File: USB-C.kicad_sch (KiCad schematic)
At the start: 8 parts, among them J2 HRO_TYPE-C-31-M-12, U3 USBLC6-2SC6

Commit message: feat(pcb): Version 0.2
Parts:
- removed U3: USBLC6-2SC6, marbastlib-various:SOT-23-6-routable, symbol Power_Protection:USBLC6-2SC6
- added U3: (no value), symbol Power_Protection:SRV05-4
- C8: value 4.7uF -> (none); footprint Capacitor_SMD:C_0603_1608Metric -> (none)
- C9: value 1uF -> (none); footprint Capacitor_SMD:C_0603_1608Metric -> (none)
- F2: value 500mA -> (none); footprint Fuse:Fuse_0603_1608Metric -> (none)
- FB1: value 120@100MHz -> (none); footprint Inductor_SMD:L_0603_1608Metric -> (none)
- J2: value HRO_TYPE-C-31-M-12 -> (none); footprint Conejo:USB_C_Receptacle_HRO_TYPE-C-31-M-12 (Reversible) -> (none)
- R8: renamed from R9; value 5K1 -> (none); footprint Resistor_SMD:R_0603_1608Metric -> (none)
- R9: renamed from R10; value 5K1 -> (none); footprint Resistor_SMD:R_0603_1608Metric -> (none)
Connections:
- net +5V: now also U3.5 (VP)
- net GND: now also U3.2 (VN)
- net DI+ renamed D+
- net D+: now also U3.4 (IO3)
- net DI- renamed D-
- net D-: now also U3.3 (IO2)

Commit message: feat(pcb): Version 0.2.1
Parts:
- C8: value (none) -> 4.7uF; footprint (none) -> Capacitor_SMD:C_0402_1005Metric
- C9: value (none) -> 1uF; footprint (none) -> Capacitor_SMD:C_0402_1005Metric
- FB1: value (none) -> 120@100MHz; footprint (none) -> Inductor_SMD:L_0402_1005Metric
- J2: value (none) -> HRO_TYPE-C-31-M-12; footprint (none) -> Athena54:USB_C_Receptacle_HRO_TYPE-C-31-M-12 (Reversible)
- R8, R9: value (none) -> 5K1; footprint (none) -> Resistor_SMD:R_0402_1005Metric
- U3: value (none) -> SRV05-4; footprint (none) -> marbastlib-various:SOT-23-6-routable
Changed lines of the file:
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@@
       (effects (font (size 1.27 1.27)) (justify right))
     )
-    (property "Value" "" (id 1) (at 75.3491 34.7158 0)
-      (effects (font (size 1.27 1.27)) (justify right))
-    )
-    (property "Footprint" "" (id 2) (at 73.025 33.02 0)
+    (property "Value" "4.7uF" (id 1) (at 75.3491 34.7158 0)
+      (effects (font (size 1.27 1.27)) (justify right))
+    )
+    (property "Footprint" "Capacitor_SMD:C_0402_1005Metric" (id 2) (at 73.025 33.02 0)
       (effects (font (size 1.27 1.27)) hide)
     )
@@
       (effects (font (size 1.27 1.27)) (justify right))
     )
-    (property "Value" "" (id 1) (at 88.0491 34.7158 0)
-      (effects (font (size 1.27 1.27)) (justify right))
-    )
-    (property "Footprint" "" (id 2) (at 85.725 33.02 0)
+    (property "Value" "1uF" (id 1) (at 88.0491 34.7158 0)
+      (effects (font (size 1.27 1.27)) (justify right))
+    )
+    (property "Footprint" "Capacitor_SMD:C_0402_1005Metric" (id 2) (at 85.725 33.02 0)
       (effects (font (size 1.27 1.27)) hide)
     )
@@
       (effects (font (size 1.27 1.27)) (justify left))
     )
-    (property "Value" "" (id 1) (at 120.2437 29.3171 0)
-      (effects (font (size 1.27 1.27)) (justify left))
-    )
-    (property "Footprint" "" (id 2) (at 135.255 52.07 0)
+    (property "Value" "SRV05-4" (id 1) (at 120.2437 29.3171 0)
+      (effects (font (size 1.27 1.27)) (justify left))
+    )
+    (property "Footprint" "marbastlib-various:SOT-23-6-routable" (id 2) (at 135.255 52.07 0)
       (effects (font (size 1.27 1.27)) hide)
     )
@@
       (effects (font (size 1.27 1.27)) (justify left))
     )
-    (property "Value" "" (id 1) (at 64.9986 41.7072 0)
-      (effects (font (size 1.27 1.27)) (justify left))
-    )
-    (property "Footprint" "" (id 2) (at 63.5 40.005 0)
+    (property "Value" "5K1" (id 1) (at 64.9986 41.7072 0)
+      (effects (font (size 1.27 1.27)) (justify left))
+    )
+    (property "Footprint" "Resistor_SMD:R_0402_1005Metric" (id 2) (at 63.5 40.005 0)
       (effects (font (size 1.27 1.27)) hide)
     )
@@
       (effects (font (size 1.27 1.27)) (justify right))
     )
-    (property "Value" "" (id 1) (at 58.8264 41.7072 0)
-      (effects (font (size 1.27 1.27)) (justify right))
-    )
-    (property "Footprint" "" (id 2) (at 60.325 40.005 0)
+    (property "Value" "5K1" (id 1) (at 58.8264 41.7072 0)
+      (effects (font (size 1.27 1.27)) (justify right))
+    )
+    (property "Footprint" "Resistor_SMD:R_0402_1005Metric" (id 2) (at 60.325 40.005 0)
       (effects (font (size 1.27 1.27)) hide)
     )
@@
     (in_bom yes) (on_board yes) (fields_autoplaced)
     (property "Reference" "J2" (id 0) (at 26.67 22.3352 0))
-    (property "Value" "" (id 1) (at 26.67 24.8721 0))
-    (property "Footprint" "" (id 2) (at 30.48 43.815 0)
+    (property "Value" "HRO_TYPE-C-31-M-12" (id 1) (at 26.67 24.8721 0))
+    (property "Footprint" "Athena54:USB_C_Receptacle_HRO_TYPE-C-31-M-12 (Reversible)" (id 2) (at 30.48 43.815 0)
       (effects (font (size 1.27 1.27)) hide)
     )
@@
     (in_bom yes) (on_board yes) (fields_autoplaced)
     (property "Reference" "FB1" (id 0) (at 63.4619 23.1734 90))
-    (property "Value" "" (id 1) (at 63.4619 25.7103 90))
-    (property "Footprint" "" (id 2) (at 63.5 30.353 90)
-      (effects (font (size 1.27 1.27)) hide)
-    )
+    (property "Value" "120@100MHz" (id 1) (at 63.4619 25.7103 90))
+    (property "Footprint" "Inductor_SMD:L_0402_1005Metric" (id 2) (at 63.5 30.353 90)
+      (effects (font (size 1.27 1.27)) hide)
+    )

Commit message: fix(schematic): Fix links to footprints
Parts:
- F2: value (none) -> 500mA; footprint (none) -> Fuse:Fuse_0603_1608Metric
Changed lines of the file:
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@@
     (in_bom yes) (on_board yes) (fields_autoplaced)
     (property "Reference" "F2" (id 0) (at 50.8 23.9862 90))
-    (property "Value" "" (id 1) (at 50.8 26.5231 90))
-    (property "Footprint" "" (id 2) (at 55.88 27.305 0)
+    (property "Value" "500mA" (id 1) (at 50.8 26.5231 90))
+    (property "Footprint" "Fuse:Fuse_0603_1608Metric" (id 2) (at 55.88 27.305 0)
       (effects (font (size 1.27 1.27)) (justify left) hide)
     )

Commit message: refactor!!!(repository): Rename from Athena54 to Conejo
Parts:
- J2: footprint Athena54:USB_C_Receptacle_HRO_TYPE-C-31-M-12 (Reversible) -> Conejo:USB_C_Receptacle_HRO_TYPE-C-31-M-12 (Reversible)
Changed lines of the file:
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@@
     (property "Reference" "J2" (id 0) (at 26.67 22.3352 0))
     (property "Value" "HRO_TYPE-C-31-M-12" (id 1) (at 26.67 24.8721 0))
-    (property "Footprint" "Athena54:USB_C_Receptacle_HRO_TYPE-C-31-M-12 (Reversible)" (id 2) (at 30.48 43.815 0)
+    (property "Footprint" "Conejo:USB_C_Receptacle_HRO_TYPE-C-31-M-12 (Reversible)" (id 2) (at 30.48 43.815 0)
       (effects (font (size 1.27 1.27)) hide)
     )

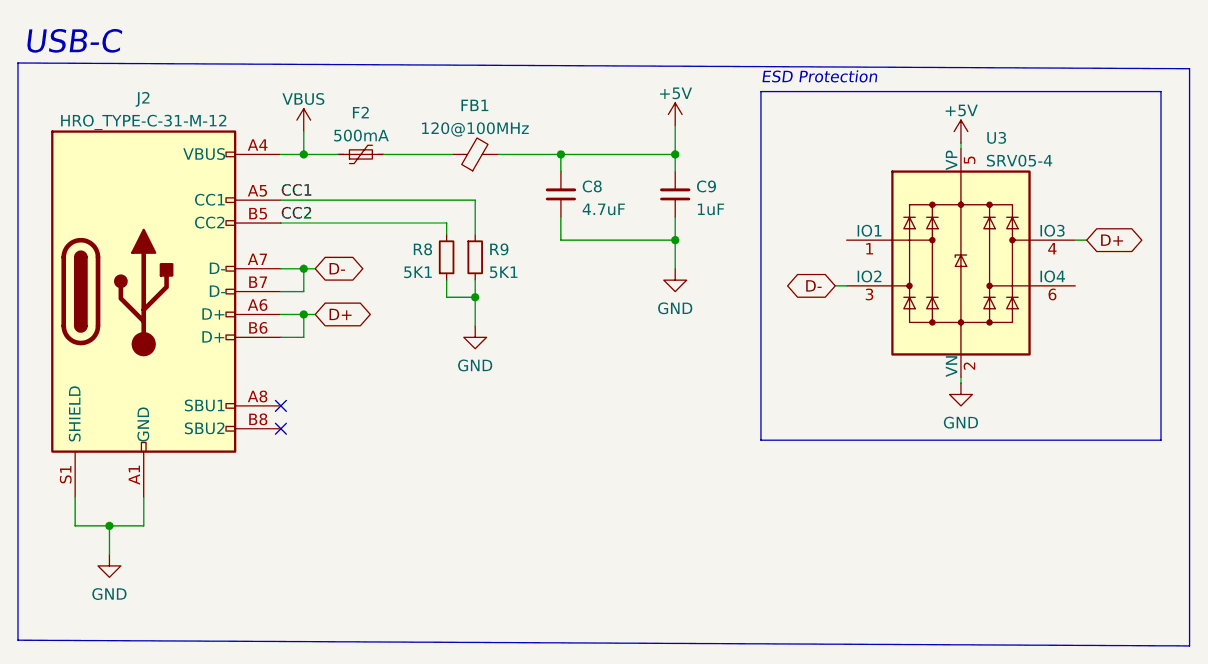
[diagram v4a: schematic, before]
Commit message: feat(pcb): Version 0.2.2
- Update MS88SF3 footprint
- Create thumb cluster silksscreen
- Separate NTPH and PTH drill files
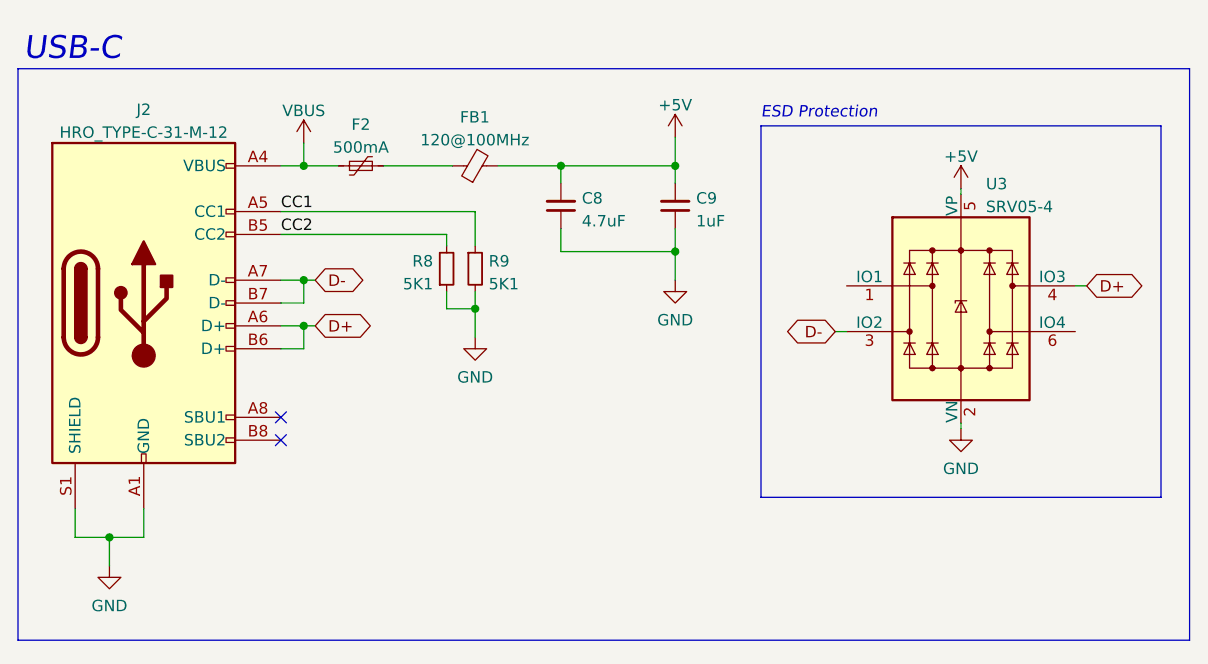
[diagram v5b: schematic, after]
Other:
- moved on the sheet: C8, C9, F2, FB1, J2, R8, R9, U3

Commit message: feat(pcb): Version 0.3
- Move components entirely to back copper :tada:
- Update silkscreen legibility to enhance ease of component placement
- Fix I2C pullup resistors
  - Replace incorrect value of 1K5 with 5K1
  - Update footprint to 0603_1608 to fit VDD traces underneath, compared to original 0402_1005 footprint
- Increase text width on RESET button, POWER Switch, and CHG LED
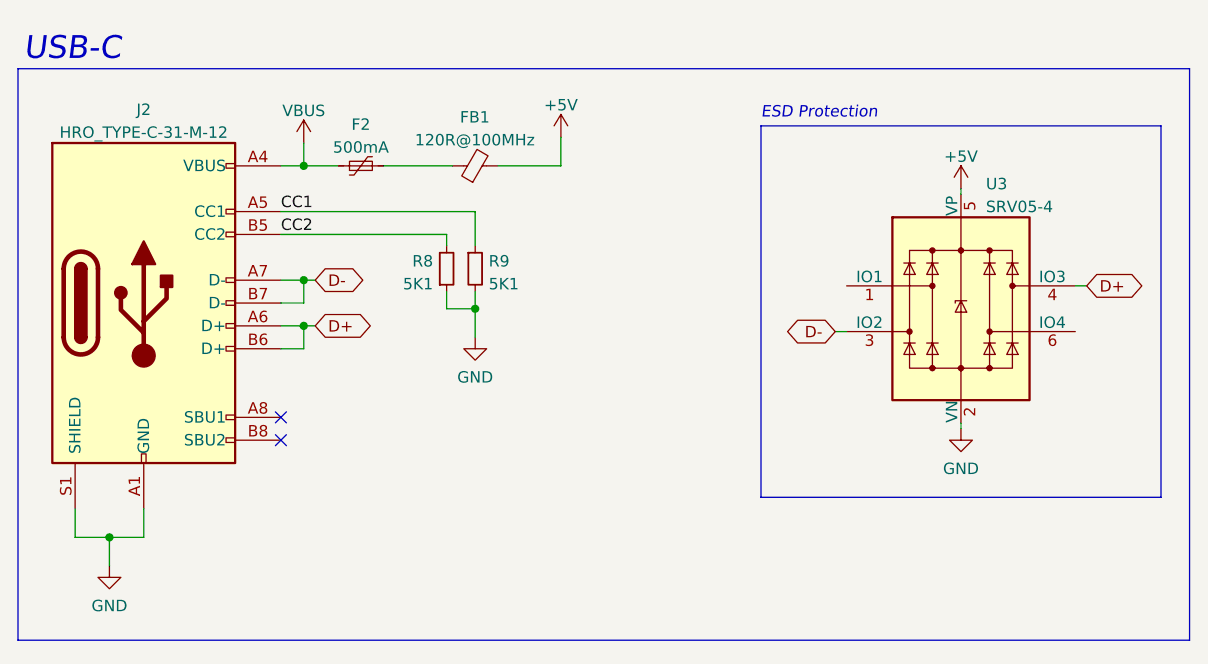
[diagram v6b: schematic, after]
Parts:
- removed C8: 4.7uF, Capacitor_SMD:C_0402_1005Metric, symbol Device:C_Small
- removed C9: 1uF, Capacitor_SMD:C_0402_1005Metric, symbol Device:C_Small
- FB1: value 120@100MHz -> 120R@100MHz
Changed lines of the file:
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@@
   (junction (at 44.45 47.625) (diameter 0) (color 0 0 0 0)
   )
-  (junction (at 73.025 29.845) (diameter 0) (color 0 0 0 0)
-  )
   (junction (at 44.45 42.545) (diameter 0) (color 0 0 0 0)
   )
-  (junction (at 85.725 39.37) (diameter 0) (color 0 0 0 0)
-  )
   (junction (at 63.5 45.72) (diameter 0) (color 0 0 0 0)
   )
   (junction (at 44.45 29.845) (diameter 0) (color 0 0 0 0)
-  )
-  (junction (at 85.725 29.845) (diameter 0) (color 0 0 0 0)
   )
   (junction (at 22.86 71.12) (diameter 0) (color 0 0 0 0)
@@
     (stroke (width 0) (type default) (color 0 0 0 0))
   )
-  (wire (pts (xy 85.725 29.845) (xy 85.725 26.67))
-    (stroke (width 0) (type default) (color 0 0 0 0))
-  )
-  (wire (pts (xy 73.025 39.37) (xy 85.725 39.37))
+  (wire (pts (xy 73.025 29.845) (xy 73.025 26.67))
     (stroke (width 0) (type default) (color 0 0 0 0))
   )
@@
     (stroke (width 0) (type default) (color 0 0 0 0))
   )
-  (wire (pts (xy 85.725 29.845) (xy 85.725 31.75))
-    (stroke (width 0) (type default) (color 0 0 0 0))
-  )
   (wire (pts (xy 41.91 47.625) (xy 44.45 47.625))
     (stroke (width 0) (type default) (color 0 0 0 0))
   )
-  (wire (pts (xy 73.025 29.845) (xy 85.725 29.845))
-    (stroke (width 0) (type default) (color 0 0 0 0))
-  )
   (wire (pts (xy 53.34 29.845) (xy 60.96 29.845))
     (stroke (width 0) (type default) (color 0 0 0 0))
@@
     (stroke (width 0) (type default) (color 0 0 0 0))
   )
-  (wire (pts (xy 73.025 36.83) (xy 73.025 39.37))
-    (stroke (width 0) (type default) (color 0 0 0 0))
-  )
   (polyline (pts (xy 95.25 66.675) (xy 95.25 25.4))
     (stroke (width 0) (type default) (color 0 0 0 0))
@@
     (stroke (width 0) (type default) (color 0 0 0 0))
   )
-  (wire (pts (xy 85.725 42.545) (xy 85.725 39.37))
-    (stroke (width 0) (type default) (color 0 0 0 0))
-  )
   (wire (pts (xy 117.475 32.385) (xy 117.475 33.02))
     (stroke (width 0) (type default) (color 0 0 0 0))
@@
   )
   (wire (pts (xy 60.325 45.72) (xy 63.5 45.72))
-    (stroke (width 0) (type default) (color 0 0 0 0))
-  )
-  (wire (pts (xy 73.025 29.845) (xy 73.025 31.75))
-    (stroke (width 0) (type default) (color 0 0 0 0))
-  )
-  (wire (pts (xy 85.725 36.83) (xy 85.725 39.37))
     (stroke (width 0) (type default) (color 0 0 0 0))
   )
@@
     )
   )
-  (symbol (lib_id "Device:C_Small") (at 73.025 34.29 180) (unit 1)
-    (in_bom yes) (on_board yes)
-    (property "Reference" "C8" (id 0) (at 75.3491 33.4489 0)
-      (effects (font (size 1.27 1.27)) (justify right))
-    )
-    (property "Value" "4.7uF" (id 1) (at 75.3491 35.9858 0)
-      (effects (font (size 1.27 1.27)) (justify right))
-    )
-    (property "Footprint" "Capacitor_SMD:C_0402_1005Metric" (id 2) (at 73.025 34.29 0)
-      (effects (font (size 1.27 1.27)) hide)
-    )
-    (property "Datasheet" "~" (id 3) (at 73.025 34.29 0)
-      (effects (font (size 1.27 1.27)) hide)
-    )
-    (pin "1")
-    (pin "2")
-  )
-  (symbol (lib_id "Device:C_Small") (at 85.725 34.29 180) (unit 1)
-    (in_bom yes) (on_board yes) (fields_autoplaced)
-    (property "Reference" "C9" (id 0) (at 88.0491 33.4489 0)
-      (effects (font (size 1.27 1.27)) (justify right))
-    )
-    (property "Value" "1uF" (id 1) (at 88.0491 35.9858 0)
-      (effects (font (size 1.27 1.27)) (justify right))
-    )
-    (property "Footprint" "Capacitor_SMD:C_0402_1005Metric" (id 2) (at 85.725 34.29 0)
-      (effects (font (size 1.27 1.27)) hide)
-    )
-    (property "Datasheet" "~" (id 3) (at 85.725 34.29 0)
-      (effects (font (size 1.27 1.27)) hide)
-    )
-    (pin "1")
-    (pin "2")
-  )
   (symbol (lib_id "power:GND") (at 63.5 48.895 0) (unit 1)
     (in_bom yes) (on_board yes) (fields_autoplaced)
@@
     (pin "1")
   )
-  (symbol (lib_id "power:+5V") (at 85.725 26.67 0) (unit 1)
-    (in_bom yes) (on_board yes) (fields_autoplaced)
-    (property "Reference" "#PWR0115" (id 0) (at 85.725 30.48 0)
-      (effects (font (size 1.27 1.27)) hide)
-    )
-    (property "Value" "+5V" (id 1) (at 85.725 23.0942 0))
-    (property "Footprint" "" (id 2) (at 85.725 26.67 0)
-      (effects (font (size 1.27 1.27)) hide)
-    )
-    (property "Datasheet" "" (id 3) (at 85.725 26.67 0)
-      (effects (font (size 1.27 1.27)) hide)
-    )
-    (pin "1")
-  )
-  (symbol (lib_id "power:GND") (at 85.725 42.545 0) (unit 1)
-    (in_bom yes) (on_board yes) (fields_autoplaced)
-    (property "Reference" "#PWR0118" (id 0) (at 85.725 48.895 0)
-      (effects (font (size 1.27 1.27)) hide)
-    )
-    (property "Value" "GND" (id 1) (at 85.725 46.9884 0))
-    (property "Footprint" "" (id 2) (at 85.725 42.545 0)
-      (effects (font (size 1.27 1.27)) hide)
-    )
-    (property "Datasheet" "" (id 3) (at 85.725 42.545 0)
+  (symbol (lib_id "power:+5V") (at 73.025 26.67 0) (unit 1)
+    (in_bom yes) (on_board yes) (fields_autoplaced)
+    (property "Reference" "#PWR0115" (id 0) (at 73.025 30.48 0)
+      (effects (font (size 1.27 1.27)) hide)
+    )
+    (property "Value" "+5V" (id 1) (at 73.025 23.0942 0))
+    (property "Footprint" "" (id 2) (at 73.025 26.67 0)
+      (effects (font (size 1.27 1.27)) hide)
+    )
+    (property "Datasheet" "" (id 3) (at 73.025 26.67 0)
       (effects (font (size 1.27 1.27)) hide)
     )
@@
     (in_bom yes) (on_board yes) (fields_autoplaced)
     (property "Reference" "FB1" (id 0) (at 63.4619 24.4434 90))
-    (property "Value" "120@100MHz" (id 1) (at 63.4619 26.9803 90))
+    (property "Value" "120R@100MHz" (id 1) (at 63.4619 26.9803 90))
     (property "Footprint" "Inductor_SMD:L_0402_1005Metric" (id 2) (at 63.5 31.623 90)
       (effects (font (size 1.27 1.27)) hide)
